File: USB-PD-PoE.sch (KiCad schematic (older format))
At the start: 126 parts, among them J1 8P8C_Shielded, J2 8P8C_Shielded, J3 TagConnect_TC2030_SWD, J4 USB_C_Receptacle_USB2.0, Q1 FDC2512, Q2 2N7002, Q3 2N7002, Q4 2N7002, Q5 APM4953KC, T1 HR051142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

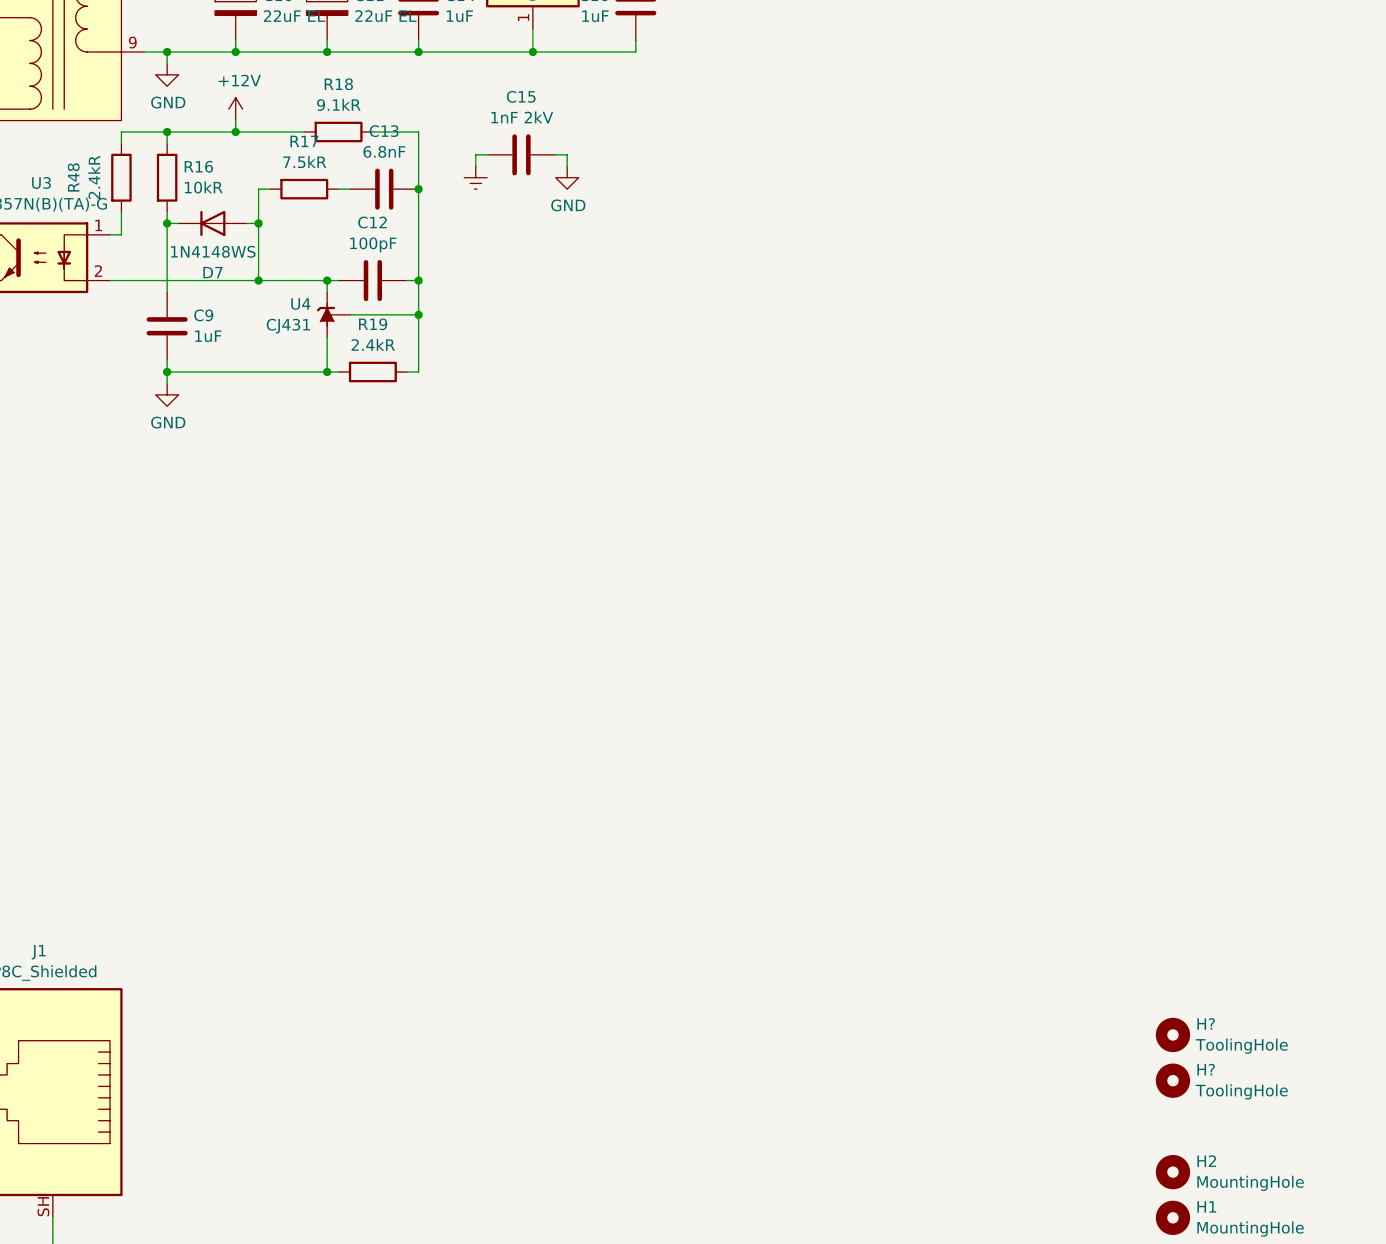
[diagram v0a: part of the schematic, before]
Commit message: Add tooling holes
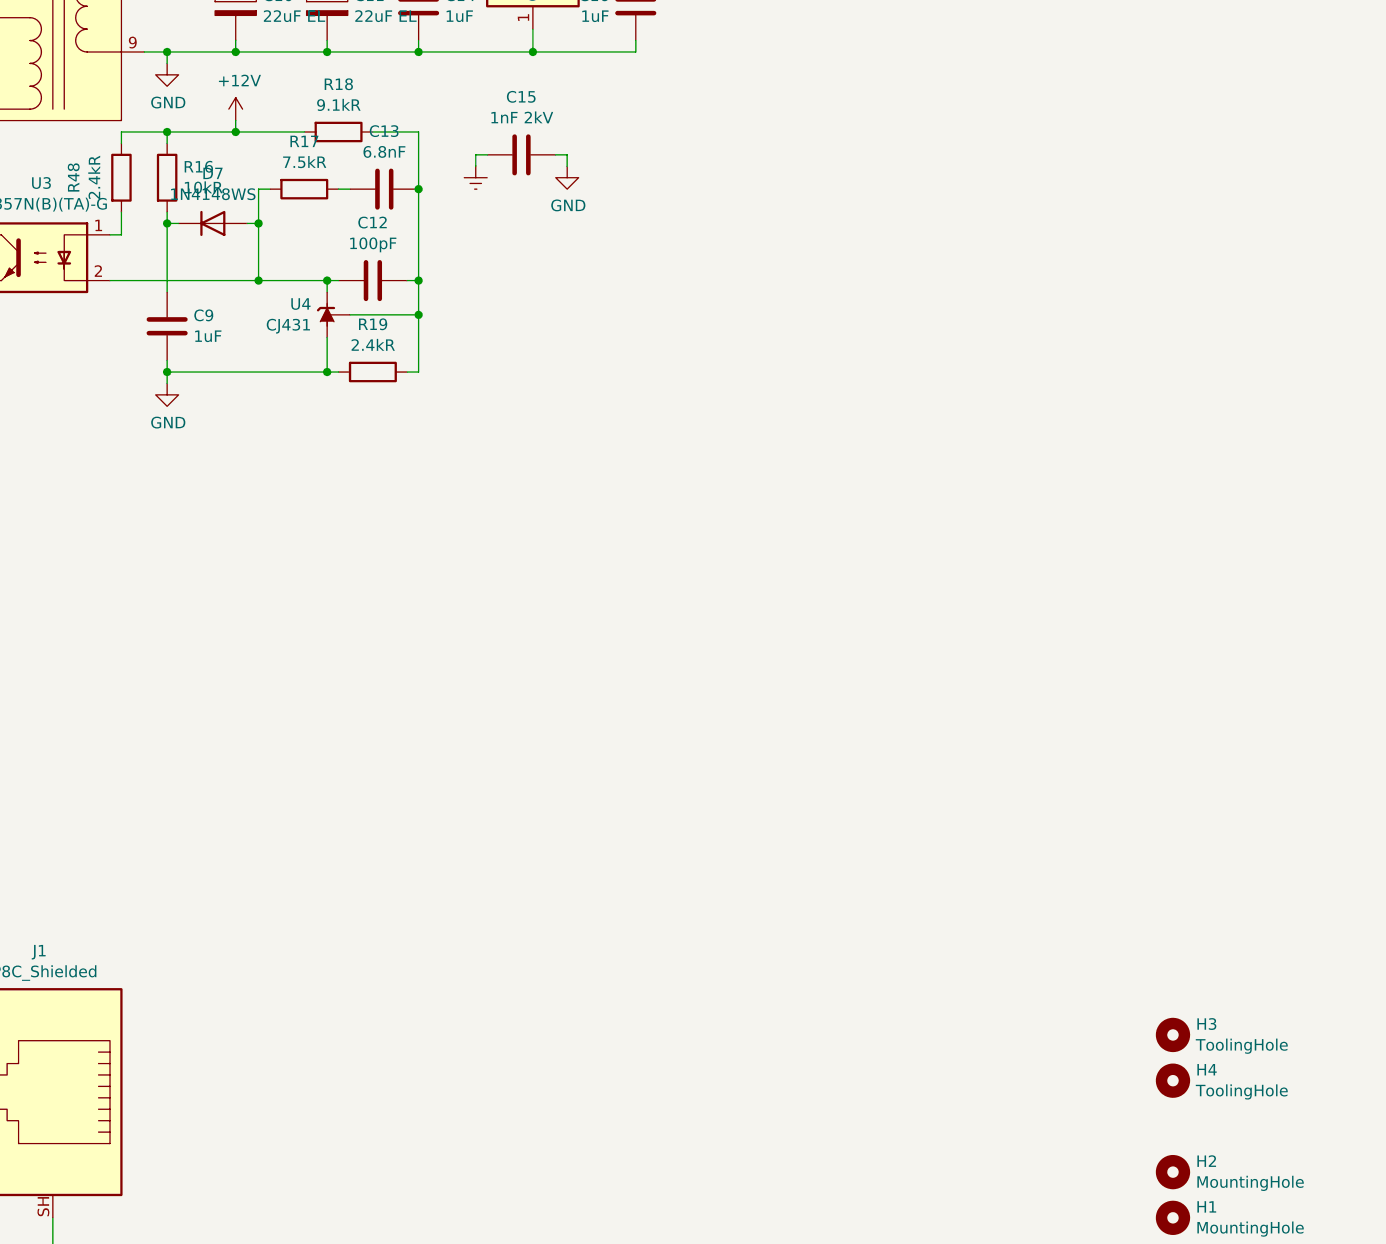
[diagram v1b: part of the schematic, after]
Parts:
- D4, D7: LCSC 1N4148WS -> C2128
- TR1: LCSC (none) -> C216359
- gave numbers to parts that had none: 2
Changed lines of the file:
@@
 F 1 "Transformer_Ethernet_QT24A01" H 3550 6826 50  0000 C CNN
 F 2 "Transformer_SMD_TNK:Transformer_Ethernet_TNK_QT24A01" H 3600 6800 50  0001 C CNN
-F 3 "" H 3600 6800 50  0001 C CNN
+F 3 "https://datasheet.lcsc.com/szlcsc/TNK-QT24A01_C216359.pdf" H 3600 6800 50  0001 C CNN
+F 4 "C216359" H 3550 5850 50  0001 C CNN "LCSC"
 	1    3550 5850
 	-1   0    0    -1
@@
 F 2 "Diode_SMD:D_SOD-323F" H 4200 1100 50  0001 C CNN
 F 3 "~" H 4200 1100 50  0001 C CNN
-F 4 "1N4148WS" H 4200 1100 50  0001 C CNN "LCSC"
+F 4 "C2128" H 4200 1100 50  0001 C CNN "LCSC"
 	1    4200 1100
 	1    0    0    -1
@@
 U 1 1 60A88AC8
 P 6350 2000
-F 0 "D7" H 6350 2217 50  0000 C CNN
-F 1 "1N4148WS" H 6350 2126 50  0000 C CNN
+F 0 "D7" H 6350 1783 50  0000 C CNN
+F 1 "1N4148WS" H 6350 1874 50  0000 C CNN
 F 2 "Diode_SMD:D_SOD-323F" H 6350 2000 50  0001 C CNN
 F 3 "~" H 6350 2000 50  0001 C CNN
-F 4 "1N4148WS" H 6350 2000 50  0001 C CNN "LCSC"
+F 4 "C2128" H 6350 2000 50  0001 C CNN "LCSC"
 	1    6350 2000
 	1    0    0    1
@@
 $EndComp
 $Comp
-L Mechanical:MountingHole H?
+L Mechanical:MountingHole H3
 U 1 1 64B5DEFD
 P 10550 5550
-F 0 "H?" H 10650 5596 50  0000 L CNN
+F 0 "H3" H 10650 5596 50  0000 L CNN
 F 1 "ToolingHole" H 10650 5505 50  0000 L CNN
 F 2 "ToolingHole:ToolingHole_JLCSMT" H 10550 5550 50  0001 C CNN
@@
 $EndComp
 $Comp
-L Mechanical:MountingHole H?
+L Mechanical:MountingHole H4
 U 1 1 64BA74DD
 P 10550 5750
-F 0 "H?" H 10650 5796 50  0000 L CNN
+F 0 "H4" H 10650 5796 50  0000 L CNN
 F 1 "ToolingHole" H 10650 5705 50  0000 L CNN
 F 2 "ToolingHole:ToolingHole_JLCSMT" H 10550 5750 50  0001 C CNN

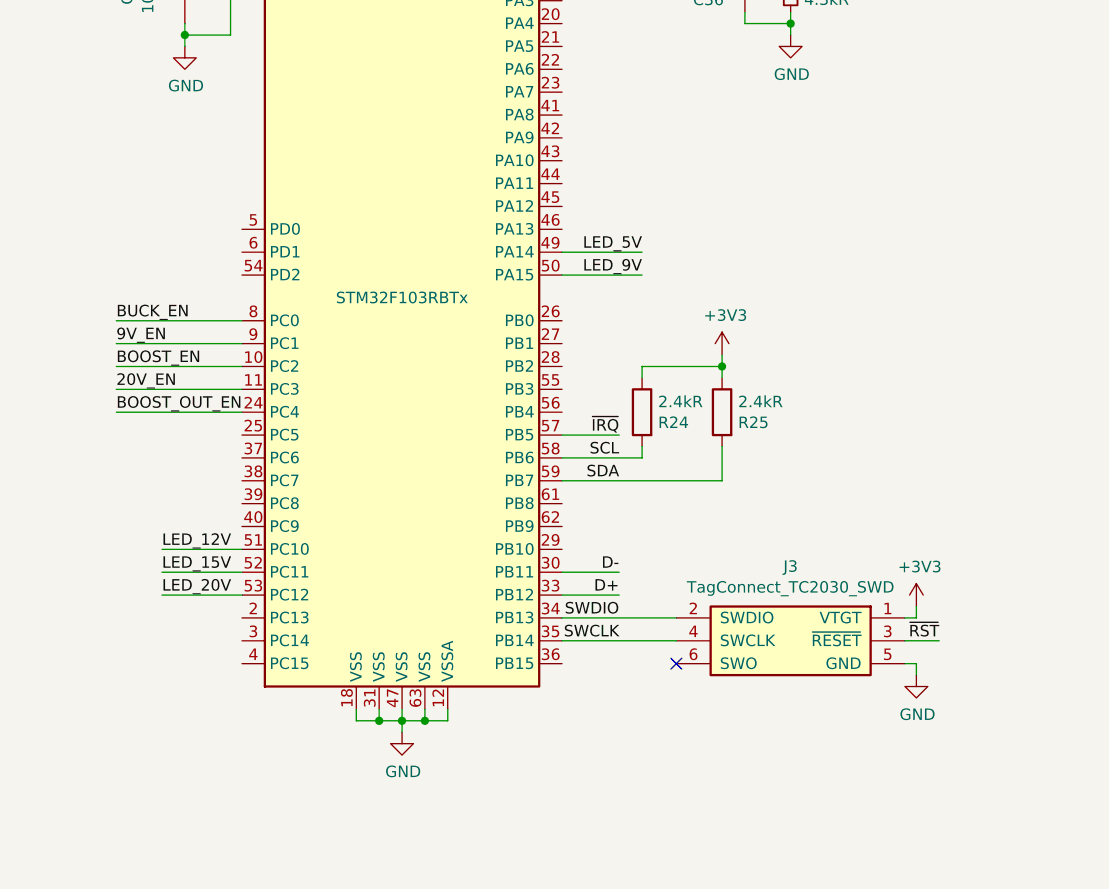
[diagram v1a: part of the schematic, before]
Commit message: Fix PA <-> PB mixup
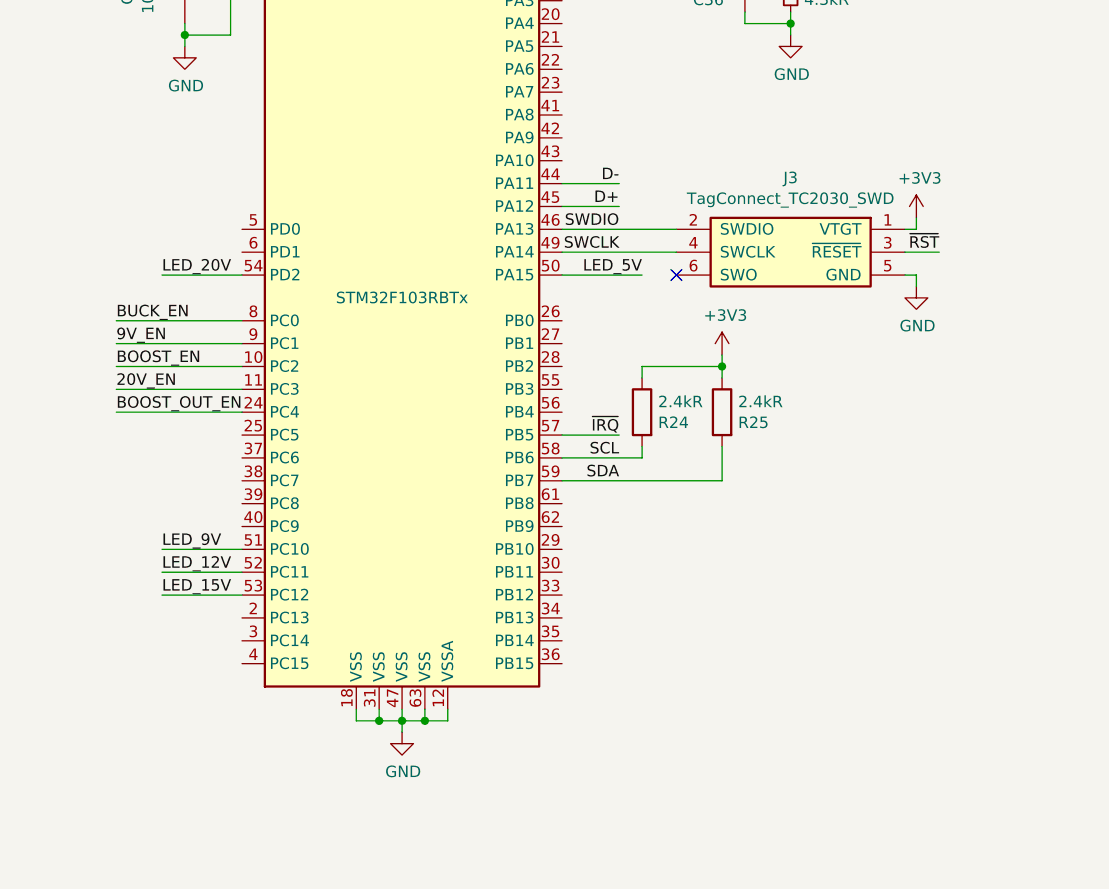
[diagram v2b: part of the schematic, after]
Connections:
- net D+: now also U1.45 (PA12); no longer U1.33 (PB12)
- net D-: now also U1.44 (PA11); no longer U1.30 (PB11)
- net LED_12V: now also U1.52 (PC11); no longer U1.51 (PC10)
- net LED_15V: now also U1.53 (PC12); no longer U1.52 (PC11)
- net LED_20V: now also U1.54 (PD2); no longer U1.53 (PC12)
- net LED_5V: now also U1.50 (PA15); no longer U1.49 (PA14)
- net LED_9V: now also U1.51 (PC10); no longer U1.50 (PA15)
- net SWCLK: now also U1.49 (PA14); no longer U1.35 (PB14)
- net SWDIO: now also U1.46 (PA13); no longer U1.34 (PB13)
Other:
- moved on the sheet: J3
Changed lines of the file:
@@
 L Connector_TagConnect:TagConnect_TC2030_SWD J3
 U 1 1 63ABCC47
-P -2000 6250
-F 0 "J3" H -2000 6575 50  0000 C CNN
-F 1 "TagConnect_TC2030_SWD" H -2000 6484 50  0000 C CNN
-F 2 "Connector:Tag-Connect_TC2030-IDC-NL_2x03_P1.27mm_Vertical" H -2000 6250 50  0001 C CNN
-F 3 "" H -2000 6250 50  0001 C CNN
-	1    -2000 6250
+P -2000 4550
+F 0 "J3" H -2000 4875 50  0000 C CNN
+F 1 "TagConnect_TC2030_SWD" H -2000 4784 50  0000 C CNN
+F 2 "Connector:Tag-Connect_TC2030-IDC-NL_2x03_P1.27mm_Vertical" H -2000 4550 50  0001 C CNN
+F 3 "" H -2000 4550 50  0001 C CNN
+	1    -2000 4550
 	-1   0    0    -1
 $EndComp
 Wire Wire Line
-	-3000 5950 -2750 5950
-Text Label -2750 5950 2    50   ~ 0
+	-3000 4250 -2750 4250
+Text Label -2750 4250 2    50   ~ 0
 D-
 Wire Wire Line
-	-3000 6050 -2750 6050
-Text Label -2750 6050 2    50   ~ 0
+	-3000 4350 -2750 4350
+Text Label -2750 4350 2    50   ~ 0
 D+
 Wire Wire Line
-	-2500 6150 -3000 6150
-Wire Wire Line
-	-2500 6250 -3000 6250
-NoConn ~ -2500 6350
+	-2500 4450 -3000 4450
+Wire Wire Line
+	-2500 4550 -3000 4550
+NoConn ~ -2500 4650
 $Comp
 L power:+3V3 #PWR0130
 U 1 1 63C2C345
-P -1450 6100
-F 0 "#PWR0130" H -1450 5950 50  0001 C CNN
-F 1 "+3V3" H -1435 6273 50  0000 C CNN
-F 2 "" H -1450 6100 50  0001 C CNN
-F 3 "" H -1450 6100 50  0001 C CNN
-	1    -1450 6100
-	1    0    0    -1
-$EndComp
-Wire Wire Line
-	-1450 6100 -1450 6150
-Wire Wire Line
-	-1450 6150 -1500 6150
-Text Label -1350 6250 2    50   ~ 0
+P -1450 4400
+F 0 "#PWR0130" H -1450 4250 50  0001 C CNN
+F 1 "+3V3" H -1435 4573 50  0000 C CNN
+F 2 "" H -1450 4400 50  0001 C CNN
+F 3 "" H -1450 4400 50  0001 C CNN
+	1    -1450 4400
+	1    0    0    -1
+$EndComp
+Wire Wire Line
+	-1450 4400 -1450 4450
+Wire Wire Line
+	-1450 4450 -1500 4450
+Text Label -1350 4550 2    50   ~ 0
 ~RST
 Wire Wire Line
-	-1350 6250 -1500 6250
+	-1350 4550 -1500 4550
 $Comp
 L power:GND #PWR0131
 U 1 1 63CAA8F9
-P -1450 6400
-F 0 "#PWR0131" H -1450 6150 50  0001 C CNN
-F 1 "GND" H -1445 6227 50  0000 C CNN
-F 2 "" H -1450 6400 50  0001 C CNN
-F 3 "" H -1450 6400 50  0001 C CNN
-	1    -1450 6400
-	1    0    0    -1
-$EndComp
-Wire Wire Line
-	-1450 6400 -1450 6350
-Wire Wire Line
-	-1450 6350 -1500 6350
+P -1450 4700
+F 0 "#PWR0131" H -1450 4450 50  0001 C CNN
+F 1 "GND" H -1445 4527 50  0000 C CNN
+F 2 "" H -1450 4700 50  0001 C CNN
+F 3 "" H -1450 4700 50  0001 C CNN
+	1    -1450 4700
+	1    0    0    -1
+$EndComp
+Wire Wire Line
+	-1450 4700 -1450 4650
+Wire Wire Line
+	-1450 4650 -1500 4650
 Text Label -4800 3150 0    50   ~ 0
 ~RST
@@
 Wire Wire Line
 	-6150 7150 -6150 7100
-Text Label -2650 4550 2    50   ~ 0
+Text Label -2650 4650 2    50   ~ 0
 LED_5V
-Wire Wire Line
-	-3000 4550 -2650 4550
-Text Label -2650 4650 2    50   ~ 0
-LED_9V
 Wire Wire Line
 	-3000 4650 -2650 4650
 Text Label -4750 5850 0    50   ~ 0
-LED_12V
+LED_9V
 Wire Wire Line
 	-4400 5850 -4750 5850
 Text Label -4750 5950 0    50   ~ 0
-LED_15V
+LED_12V
 Wire Wire Line
 	-4400 5950 -4750 5950
 Text Label -4750 6050 0    50   ~ 0
+LED_15V
+Wire Wire Line
+	-4400 6050 -4750 6050
+Text Label -4750 4650 0    50   ~ 0
 LED_20V
 Wire Wire Line
-	-4400 6050 -4750 6050
+	-4400 4650 -4750 4650
 Text Label -6500 6450 3    50   ~ 0
 LED_12V
@@
 Wire Wire Line
 	-2300 5050 -2300 5100
-Text Label -2750 6150 2    50   ~ 0
+Text Label -2750 4450 2    50   ~ 0
 SWDIO
-Text Label -2750 6250 2    50   ~ 0
+Text Label -2750 4550 2    50   ~ 0
 SWCLK
 $Comp

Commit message: Protect screw holes from layer shorts
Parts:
- H2: footprint MountingHole:MountingHole_3.2mm_M3 -> MountingHole:MountingHole_3.2mm_M3_Pad_Via
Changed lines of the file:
@@
 F 0 "H2" H 10650 6196 50  0000 L CNN
 F 1 "MountingHole" H 10650 6105 50  0000 L CNN
-F 2 "MountingHole:MountingHole_3.2mm_M3" H 10550 6150 50  0001 C CNN
+F 2 "MountingHole:MountingHole_3.2mm_M3_Pad_Via" H 10550 6150 50  0001 C CNN
 F 3 "~" H 10550 6150 50  0001 C CNN
 	1    10550 6150
